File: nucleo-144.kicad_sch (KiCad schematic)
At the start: 1 part, among them U4 NUCLEO144-H743ZI

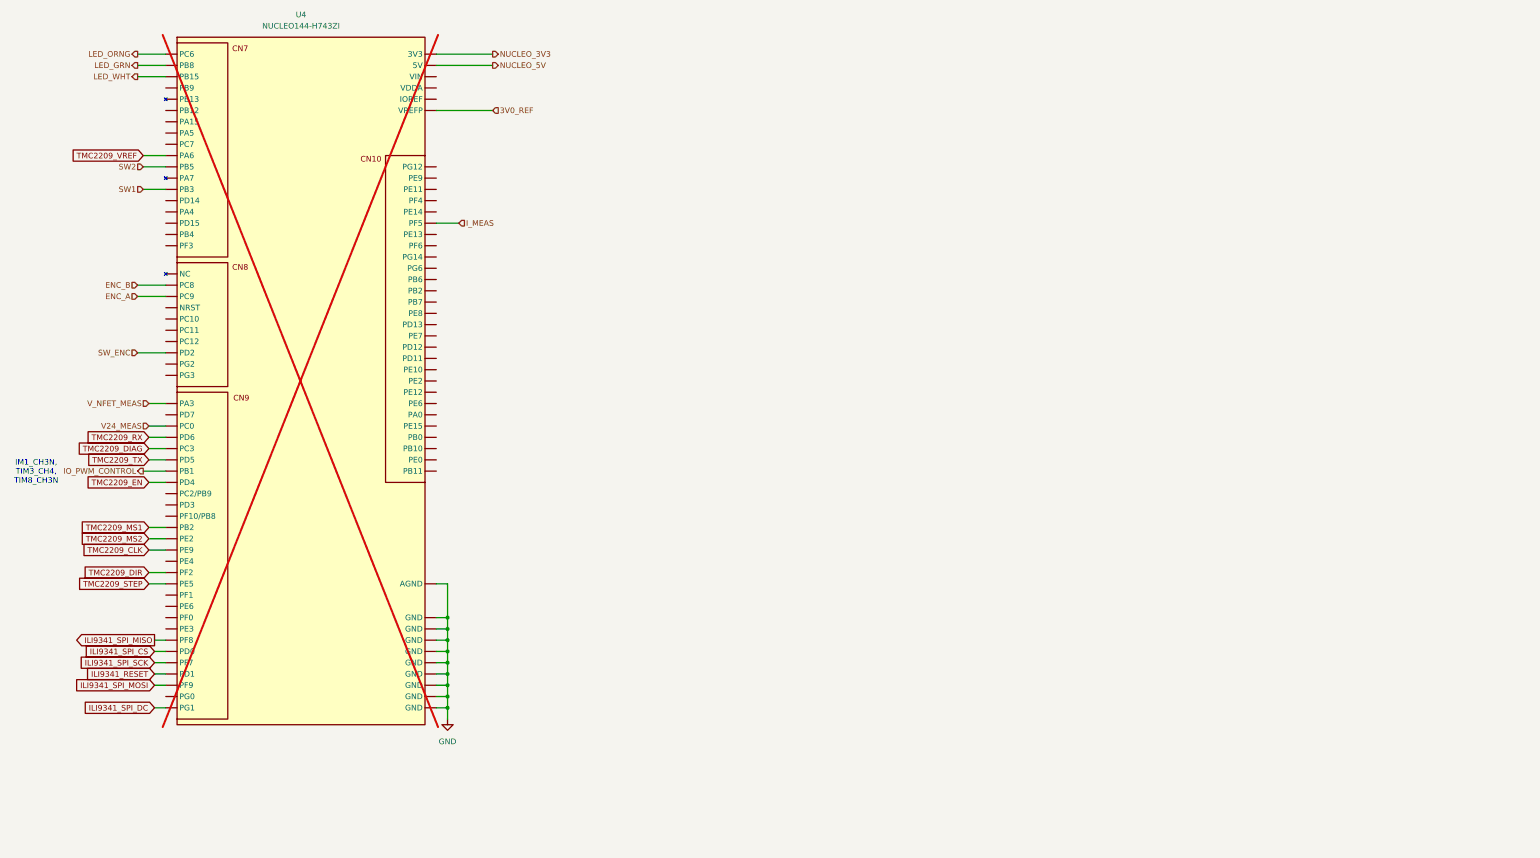
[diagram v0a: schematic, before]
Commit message: Cleaned up unecessary HMI, optimized sheets.
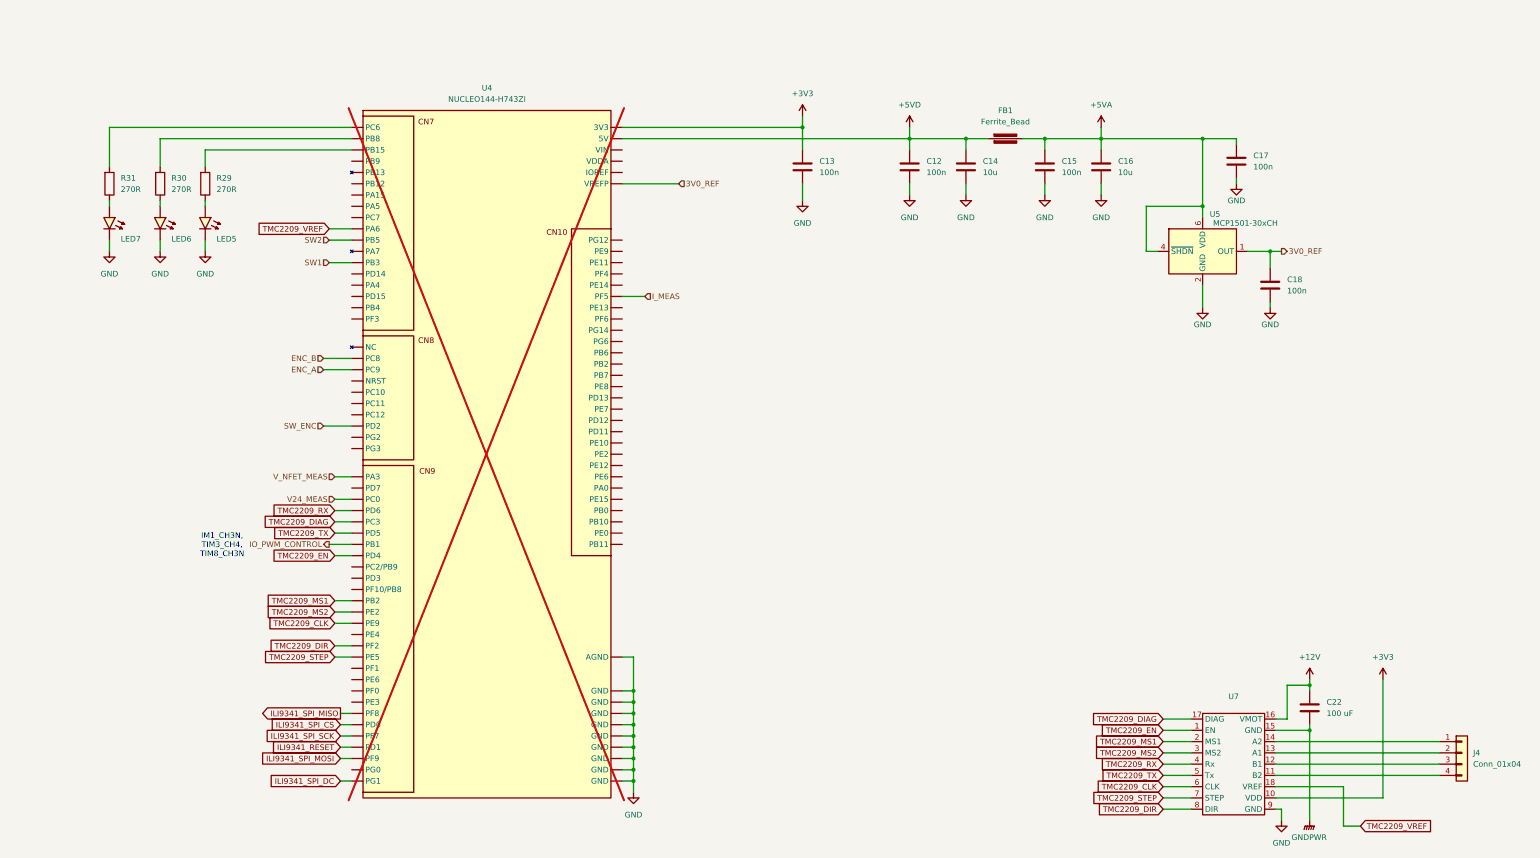
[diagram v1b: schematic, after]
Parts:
- added C12, C13, C15, C17, C18: 100n, PCM_Capacitor_SMD_AKL:C_0603_1608Metric, symbol PCM_Capacitor_AKL:C_0603
- added C14, C16: 10u, PCM_Capacitor_SMD_AKL:C_0805_2012Metric, symbol PCM_Capacitor_AKL:C_0805
- added C22: 100 uF, PCM_Capacitor_SMD_AKL:C_Elec_6.3x7.7, symbol PCM_Capacitor_AKL:C_Bipolar_SMD_D6.3mm_H5.8mm
- added FB1: Ferrite_Bead, PCM_Ferrite_SMD_AKL:Ferrite_0603_1608Metric, symbol PCM_Device_AKL:Ferrite_Bead
- added J4: Conn_01x04, Connector_JST:JST_PH_S4B-PH-K_1x04_P2.00mm_Horizontal, symbol Connector_Generic:Conn_01x04
- added LED5, LED6, LED7: ORANGE, PCM_LED_SMD_AKL:LED_0805_2012Metric, symbol PCM_LED_AKL:LED_0805_Orange
- added R29, R30, R31: 270R, PCM_Resistor_SMD_AKL:R_0603_1608Metric, symbol PCM_Resistor_AKL:R_0603
- added U5: MCP1501-30xCH, Package_TO_SOT_SMD:SOT-23-6, symbol Reference_Voltage:MCP1501-30xCH
- added U7: (no value), athaniss-device:BTT-TMC2209-V1.3_RAISED, symbol athanniss-lib:BTT-TMC2209-V1.3
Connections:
- net 3V0_REF: now also C18.1, U5.1 (OUT)
- net GND: now also C12.2, C13.2, C14.2, C15.2, C16.2, C17.2, C18.2, LED5.1 (K), LED6.1 (K), LED7.1 (K), U5.2 (GND), U5.3 (GND), U5.5 (GND), U7.9 (GND)
- net TMC2209_CLK: now also U7.6 (CLK)
- net TMC2209_DIAG: now also U7.17 (DIAG)
- net TMC2209_DIR: now also U7.8 (DIR)
- net TMC2209_EN: now also U7.1 (EN)
- net TMC2209_MS1: now also U7.2 (MS1)
- net TMC2209_MS2: now also U7.3 (MS2)
- net TMC2209_RX: now also U7.4 (Rx)
- net TMC2209_STEP: now also U7.7 (STEP)
- net TMC2209_TX: now also U7.5 (Tx)
- net TMC2209_VREF: now also U7.18 (VREF)
- net LED_GRN: no longer names the net of U4.CN7_2 (PB8)
- net LED_GRN: now also R30.1
- net LED_ORNG: no longer names the net of U4.CN7_1 (PC6)
- net LED_ORNG: now also R31.1
- net LED_WHT: no longer names the net of U4.CN7_3 (PB15)
- net LED_WHT: now also R29.1
- net NUCLEO_3V3 renamed +3V3
- net +3V3: now also C13.1, U7.10 (VDD)
- net NUCLEO_5V renamed +5VD
- net +5VD: now also C12.1, C14.1, FB1.1
- new net: LED5.2 (A), R29.2
- new net: LED7.2 (A), R31.2
- new net: J4.4 (Pin_4), U7.11 (B2)
- new net: J4.3 (Pin_3), U7.12 (B1)
- new net: J4.2 (Pin_2), U7.13 (A1)
- new net: J4.1 (Pin_1), U7.14 (A2)
- new net: LED6.2 (A), R30.2
- new net +12V: C22.1, U7.16 (VMOT)
- new net +5VA: C15.1, C16.1, C17.1, FB1.2, U5.4 (~{SHDN}), U5.6 (VDD)
- new net GNDPWR: C22.2, U7.15 (GND)
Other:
- title: (none) -> Procyon [Capstone]
- moved on the sheet: U4

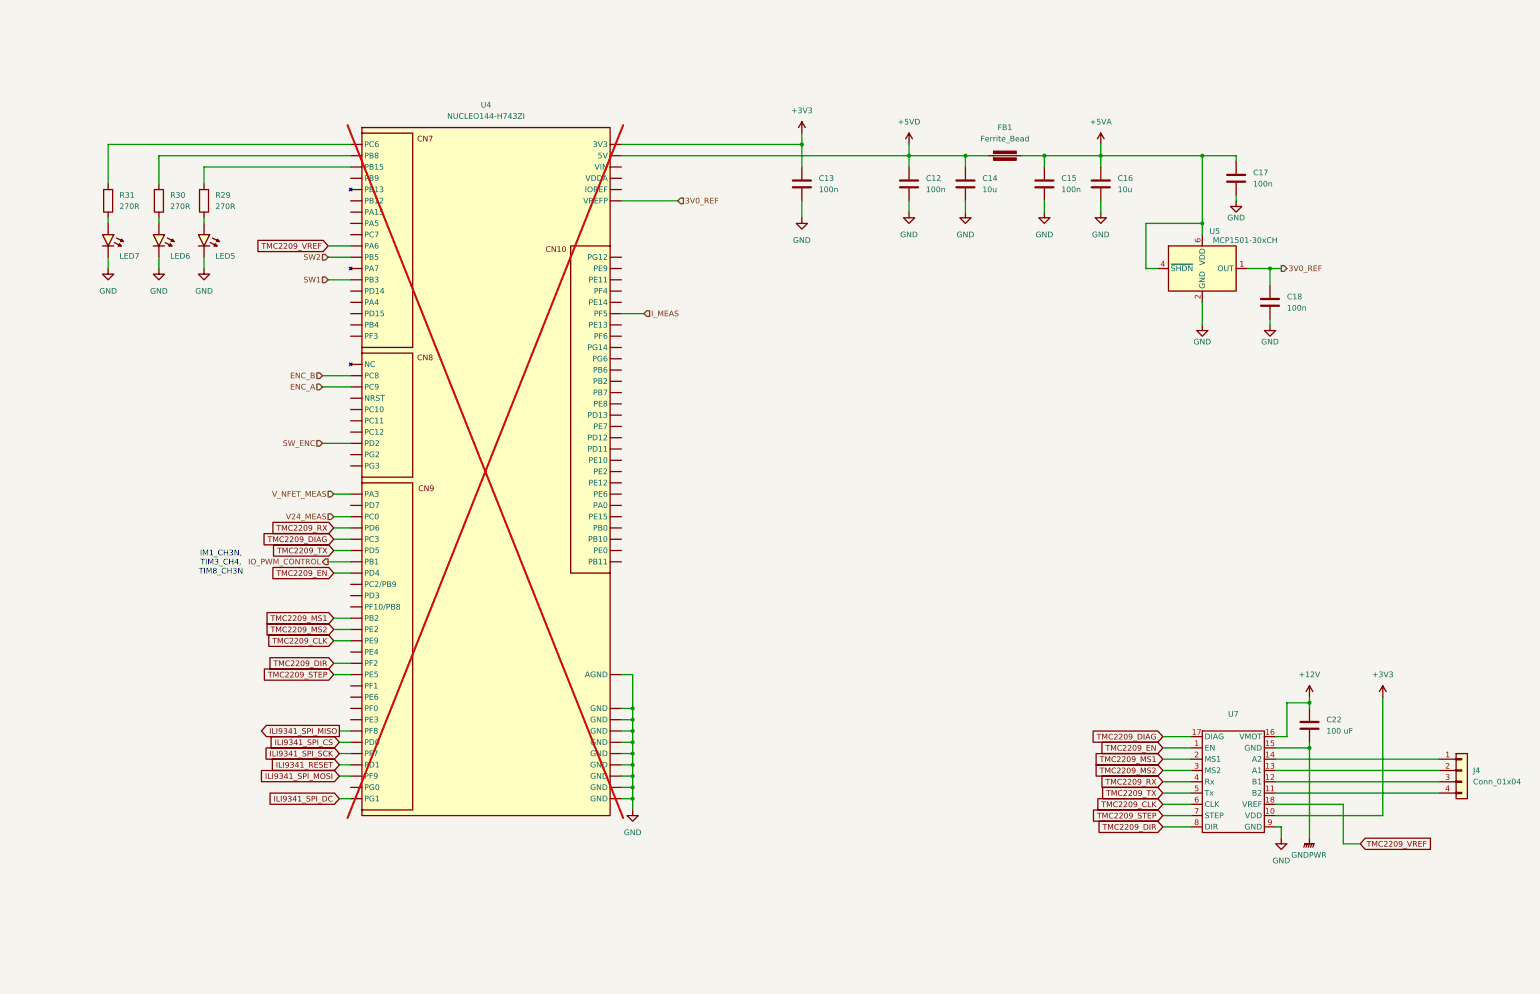
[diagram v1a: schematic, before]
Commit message: Refactored Nucleo sheet. Added back my library. Started minor work on the PCB.
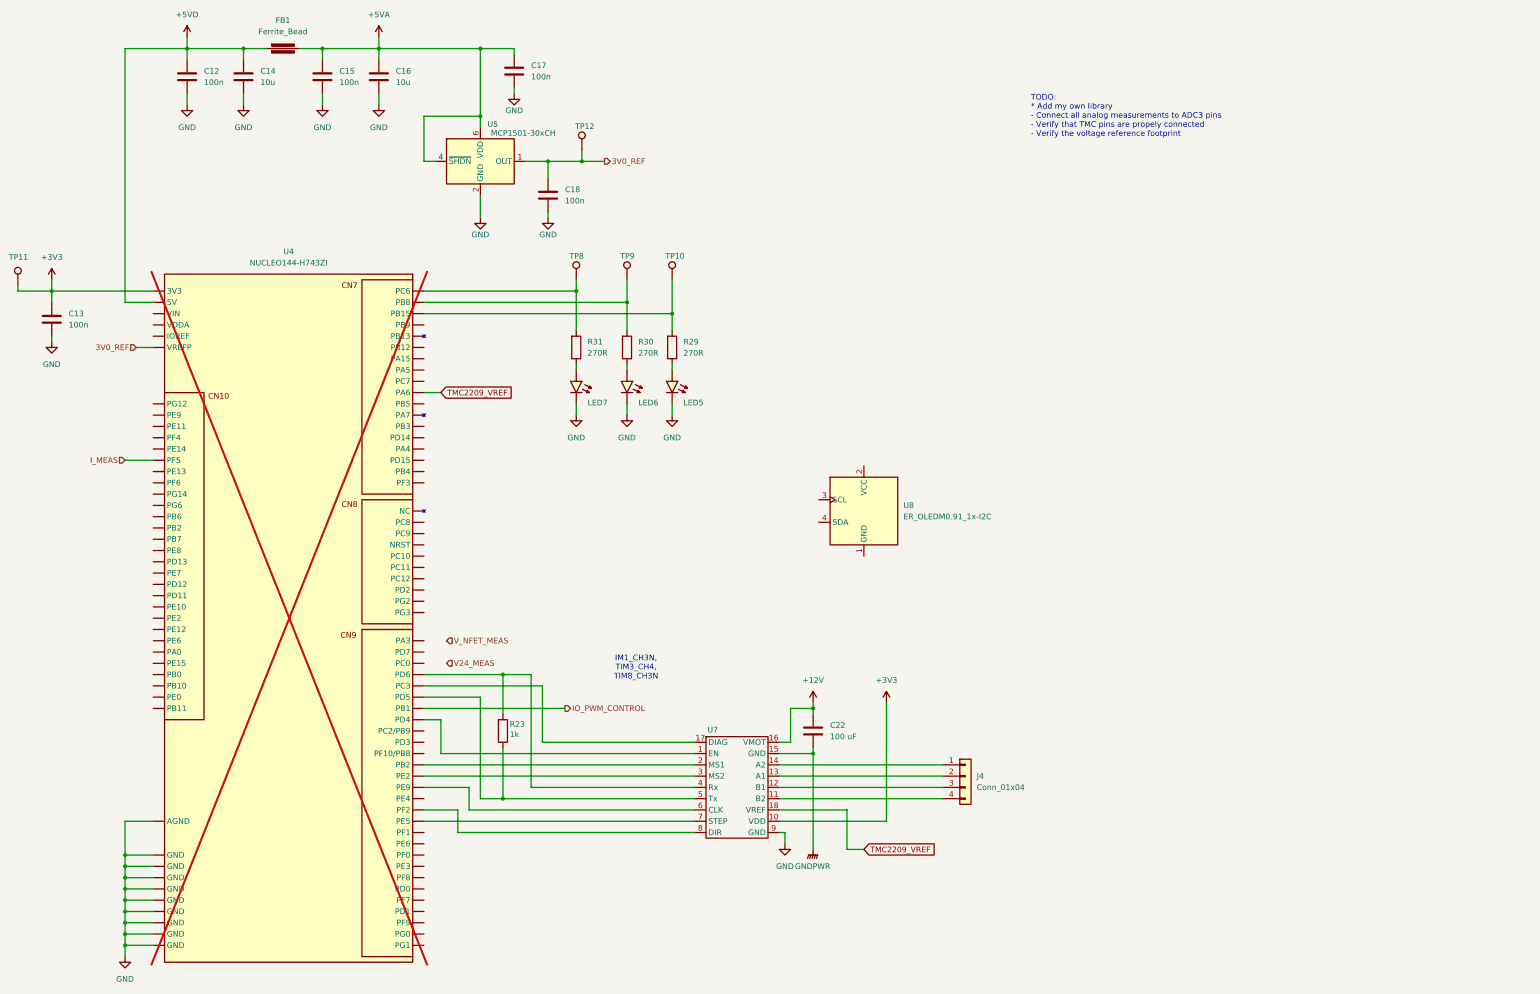
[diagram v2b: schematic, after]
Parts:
- added R23: 1k, PCM_Resistor_SMD_AKL:R_0603_1608Metric, symbol PCM_Resistor_AKL:R_0603
- added TP10, TP11, TP12, TP8, TP9: TestPoint, Connector_PinHeader_2.00mm:PinHeader_1x01_P2.00mm_Vertical, symbol Connector:TestPoint
- added U8: ER_OLEDM0.91_1x-I2C, Display:ER_OLEDM0.91_1x-I2C, symbol Display_Graphic:ER_OLEDM0.91_1x-I2C
- C22: footprint PCM_Capacitor_SMD_AKL:C_Elec_6.3x7.7 -> PCM_Capacitor_SMD_AKL:C_Elec_6.3x5.8
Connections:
- net +3V3: now also TP11.1
- net 3V0_REF: now also TP12.1
- net V24_MEAS: no longer U4.CN9_3 (PC0)
- net V_NFET_MEAS: no longer U4.CN9_1 (РАЗ)
- net at R29.1, U4.CN7_3 (PB15): now also TP10.1
- net at R31.1, U4.CN7_1 (PC6): now also TP8.1
- net at R30.1, U4.CN7_2 (PB8): now also TP9.1
- net ENC_A: no longer names the net of U4.CN8_4 (PC9)
- net ENC_B: no longer names the net of U4.CN8_2 (PC8)
- net ILI9341_RESET: no longer names the net of U4.CN9_27 (PD1)
- net ILI9341_SPI_CS: no longer names the net of U4.CN9_25 (PD0)
- net ILI9341_SPI_DC: no longer names the net of U4.CN9_30 (PG1)
- net ILI9341_SPI_MISO: no longer names the net of U4.CN9_24 (PF8)
- net ILI9341_SPI_MOSI: no longer names the net of U4.CN9_28 (PF9)
- net ILI9341_SPI_SCK: no longer names the net of U4.CN9_26 (PF7)
- net SW1: no longer names the net of U4.CN7_15 (PB3)
- net SW2: no longer names the net of U4.CN7_13 (PB5)
- net SW_ENC: no longer names the net of U4.CN8_12 (PD2)
- net TMC2209_CLK: no longer names the net of U4.CN9_15 (РЕ9), U7.6 (CLK)
- net TMC2209_DIAG: no longer names the net of U4.CN9_5 (РСЗ), U7.17 (DIAG)
- net TMC2209_DIR: no longer names the net of U4.CN9_17 (PF2), U7.8 (DIR)
- net TMC2209_EN: no longer names the net of U4.CN9_8 (PD4), U7.1 (EN)
- net TMC2209_MS1: no longer names the net of U4.CN9_13 (РВ2), U7.2 (MS1)
- net TMC2209_MS2: no longer names the net of U4.CN9_14 (PE2), U7.3 (MS2)
- net TMC2209_RX: no longer names the net of U4.CN9_4 (PD6), U7.4 (Rx)
- net TMC2209_RX: now also R23.1
- net TMC2209_STEP: no longer names the net of U4.CN9_18 (РЕ5), U7.7 (STEP)
- net TMC2209_TX: no longer names the net of U4.CN9_6 (PD5), U7.5 (Tx)
- net TMC2209_TX: now also R23.2
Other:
- note added: "TODO: * Add my own library - Connect all analog measurements to ADC3 pins - Verify that TMC pins are propely connected - Verify the voltage reference footprint"
- moved on the sheet: C12, C13, C14, C15, C16, C17, C18, C22, FB1, J4, LED5, LED6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

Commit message: Added K-type probe temperature frontend. Fixed/refactored schematics.
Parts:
- removed U5: MCP1501-30xCH, Package_TO_SOT_SMD:SOT-23-6, symbol Reference_Voltage:MCP1501-30xCH
- added C23, C24, C25: 100n, PCM_Capacitor_SMD_AKL:C_0603_1608Metric, symbol PCM_Capacitor_AKL:C_0603
- added C26: u1, PCM_Capacitor_SMD_AKL:C_0603_1608Metric, symbol PCM_Capacitor_AKL:C_0603
- added C27: 10n, PCM_Capacitor_SMD_AKL:C_0603_1608Metric, symbol PCM_Capacitor_AKL:C_0603
- added J2: Conn_01x02, Connector_JST:JST_PH_S2B-PH-K_1x02_P2.00mm_Horizontal, symbol Connector_Generic:Conn_01x02
- added J5: Conn_01x04, Connector_JST:JST_PH_S4B-PH-K_1x04_P2.00mm_Horizontal, symbol Connector_Generic:Conn_01x04
- added J6: Conn_01x03, Connector_JST:JST_PH_S3B-PH-K_1x03_P2.00mm_Horizontal, symbol Connector_Generic:Conn_01x03
- added R32, R33: 270R, PCM_Resistor_SMD_AKL:R_0603_1608Metric, symbol PCM_Resistor_AKL:R_0603
- added R36: 1k, PCM_Resistor_SMD_AKL:R_0603_1608Metric, symbol PCM_Resistor_AKL:R_0603
- added R37: 10k, PCM_Resistor_SMD_AKL:R_0603_1608Metric, symbol PCM_Resistor_AKL:R_0603
- added R38, R39: (no value), PCM_Resistor_SMD_AKL:R_0603_1608Metric, symbol PCM_Resistor_AKL:R_0603
- added TP13, TP14: TestPoint, Connector_PinHeader_2.00mm:PinHeader_1x01_P2.00mm_Vertical, symbol Connector:TestPoint
- added U10: MCP1501-33xSN, Package_SO:SOIC-8_3.9x4.9mm_P1.27mm, symbol Reference_Voltage:MCP1501-33xSN
- added U9: MCP96xx01x-x-MX, Package_DFN_QFN:QFN-20-1EP_5x5mm_P0.65mm_EP3.35x3.35mm, symbol Sensor_Temperature:MCP96xx01x-x-MX
- C18: value 100n -> 1n
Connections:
- net +3V3: now also U8.2 (VCC), C23.1, C25.1, C26.1, J5.1 (Pin_1), J6.2 (Pin_2), R37.1, R38.1, R39.1, U9.8 (V_{DD})
- net +5VA: now also U10.1 (VDD), U10.3 (~{SHDN})
- net 3V0_REF: now also U10.7 (OUT), U10.8 (FB)
- net GND: now also U8.1 (GND), C23.2, C25.2, C26.2, C27.2, J5.2 (Pin_2), J6.3 (Pin_3), U10.2 (GND), U10.4 (GND), U10.5 (GND), U10.6 (GND), U9.16 (ADDR), U9.[1,3,5,10,13,17,18,21] (GND)
- net I2C1_SCL: now reaches U8.3 (SCL)
- net I2C1_SCL: now also U4.CN7_2 (PB8), J5.3 (Pin_3), R38.2, TP14.1, U9.19 (SCL)
- net I2C1_SDA: now reaches U8.4 (SDA)
- net I2C1_SDA: now also U4.CN7_4 (PB9), J5.4 (Pin_4), R39.2, TP13.1, U9.20 (SDA)
- net at R29.1, TP10.1: no longer U4.CN7_3 (PB15)
- net at R31.1, TP8.1: no longer U4.CN7_1 (PC6)
- net ENDSTOP_SW: now reaches U4.CN7_11 (PC7)
- net ENDSTOP_SW: now also C27.1, R36.1, R37.2
- net at R30.1, TP9.1: no longer U4.CN7_2 (PB8)
- new net: J6.1 (Pin_1), R36.2
- new net: C24.1, R32.1, U9.2 (V_{IN}+)
- new net: C24.2, R33.1, U9.4 (V_{IN}-)
- new net: J2.1 (Pin_1), R32.2
- new net: J2.2 (Pin_2), R33.2
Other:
- note added: "0.91" OLED Display"
- note added: "Endstop Switch Connector"
- note added: "External modules already have pullups, so populate as/if needed."
- note added: "I2C Connector"
- note added: "TODO: * Add my own library * Add k-type thermocouple IC * Add i2c output * Add Endstop connector * Connect endstop switch to STM32 - Connect all analog measurements to ADC3 pins * Verify that TMC pins are propely connected * Verify the voltage reference footprint - Connect LED's/outputs"
- note added: "Thermocouple"
- note removed: "TODO: * Add my own library - Connect all analog measurements to ADC3 pins - Verify that TMC pins are propely connected - Verify the voltage reference footprint"
- moved on the sheet: C12, C13, C14, C15, C16, C17, C18, C22, FB1, J4, LED5, LED6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

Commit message: Finalized V1.1. Refactor schematics (PCB is ripped up) for HS measurement. Kept LS custom chain for reference.
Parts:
- added J1: Screw_Terminal_01x02, TerminalBlock_Phoenix:TerminalBlock_Phoenix_MKDS-1,5-2-5.08_1x02_P5.08mm_Horizontal, symbol Connector:Screw_Terminal_01x02
- added TP16, TP17, TP18, TP19, TP20: TestPoint, Connector_PinHeader_2.54mm:PinHeader_1x01_P2.54mm_Vertical, symbol Connector:TestPoint
- R29, R30, R31: value 270R -> 560R
- U7: value (none) -> BTT TMC2209 V1.3
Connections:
- net +12V: now also J1.2 (Pin_2)
- net GND: now also TP16.1, TP17.1, TP18.1, TP19.1, TP20.1
- net GNDPWR: now also J1.1 (Pin_1)
- net at R29.1, TP10.1: now also U4.CN7_17 (PA4)
- net at R31.1, TP8.1: now also U4.CN7_15 (PB3)
- net ADC_IFET_HS: now reaches U4.CN10_11 (PF6)
- net at U4.CN7_16 (PD14): now also R30.1, TP9.1
- net ADC_VFET: now reaches U4.CN7_20 (PF3)
- net ADC_VBUS: now reaches U4.CN9_3 (PC0)
- net 3V0_REF renamed ADC_VREF
- net I_MEAS renamed ADC_IFET_LS
- no-connect marks 0 -> 6
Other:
- note added: "-> ADC3_INP10"
- note added: "-> ADC3_INP5"
- note added: "ADC3_INP4 ->"
- note added: "ADC3_INP8 ->"
- note added: "TIM1_CH3N, TIM3_CH4, TIM8_CH3N"
- note added: "TODO: * Add my own library * Add k-type thermocouple IC * Add i2c output * Add Endstop connector * Connect endstop switch to STM32 * Connect all analog measurements to ADC3 pins * Verify that TMC pins are propely connected * Verify the voltage reference footprint * Connect LED's/outputs * Add GND 2.54" pins!"
- note removed: "IM1_CH3N, TIM3_CH4, TIM8_CH3N"
- note removed: "TODO: * Add my own library * Add k-type thermocouple IC * Add i2c output * Add Endstop connector * Connect endstop switch to STM32 - Connect all analog measurements to ADC3 pins * Verify that TMC pins are propely connected * Verify the voltage reference footprint - Connect LED's/outputs"
- moved on the sheet: LED5, LED6, LED7, R29, R30, R31, TP10, TP8, TP9
